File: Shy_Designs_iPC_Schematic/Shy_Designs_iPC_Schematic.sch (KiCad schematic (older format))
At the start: 1 part

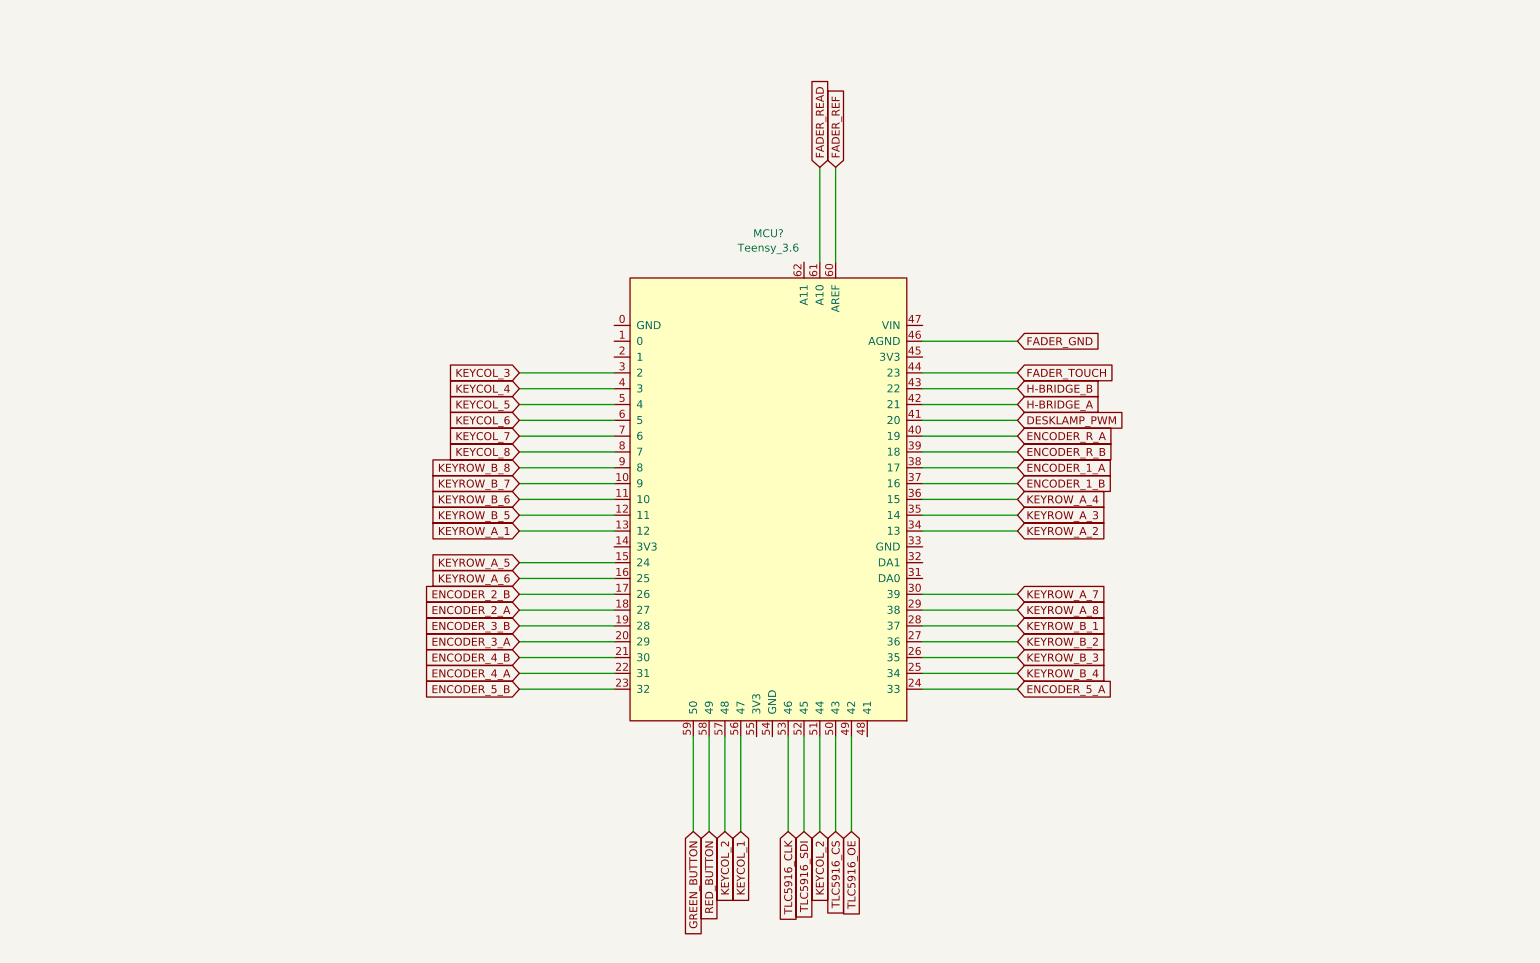
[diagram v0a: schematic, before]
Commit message: Correct schematic
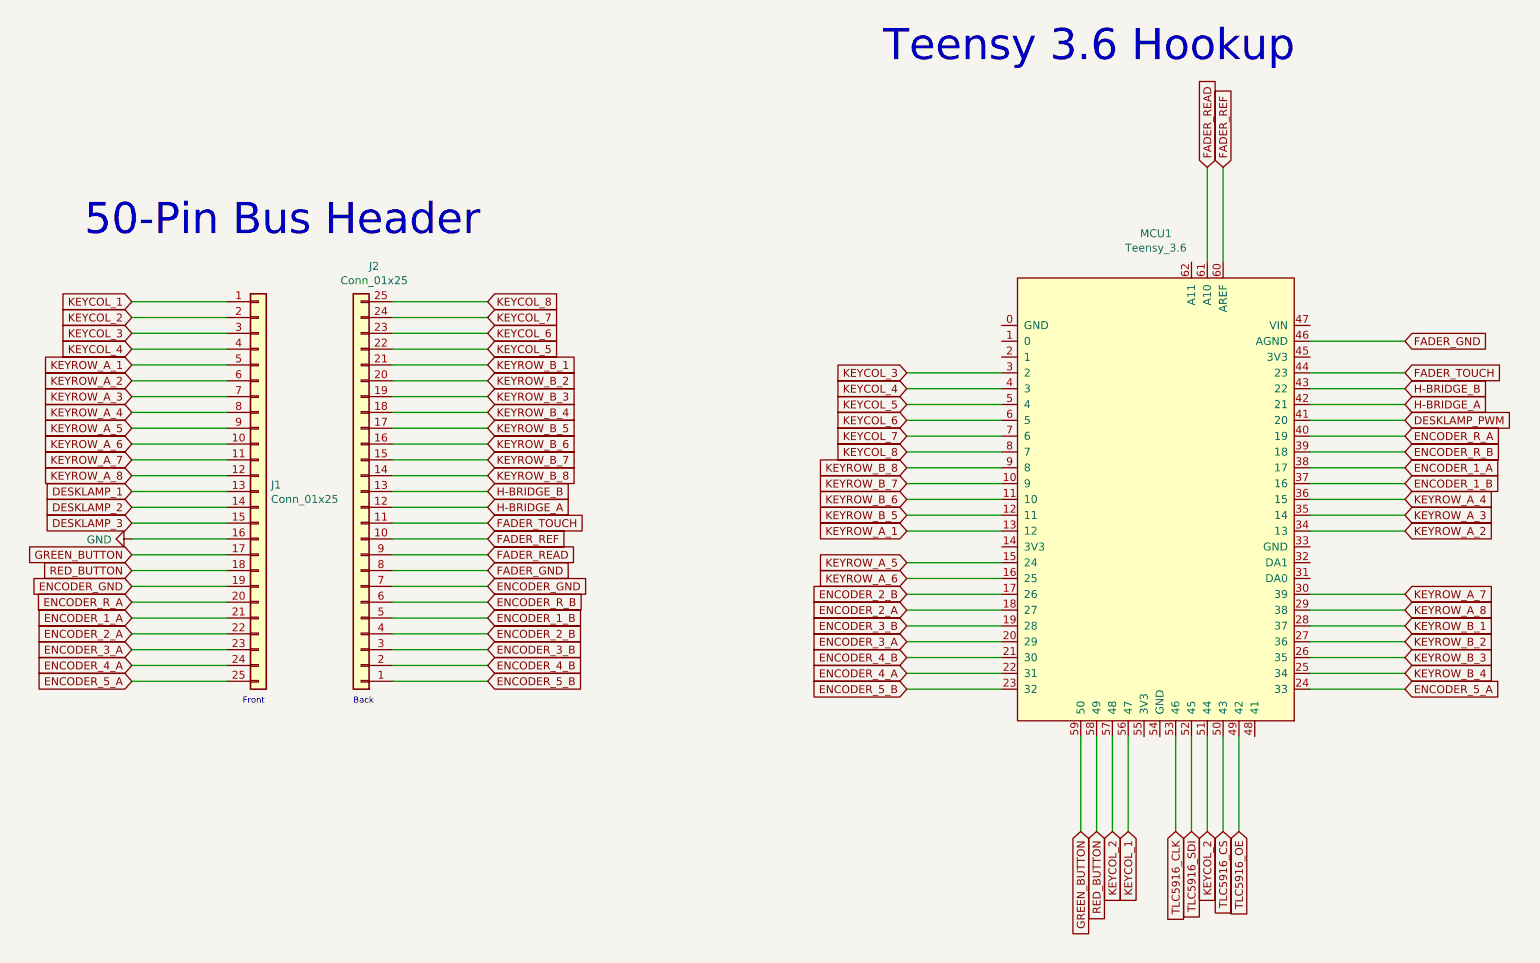
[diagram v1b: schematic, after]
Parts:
- added J1, J2: Conn_01x25, symbol Connector_Generic:Conn_01x25
- gave numbers to parts that had none: 1
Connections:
- net ENCODER_1_A: now also J1.21 (Pin_21)
- net ENCODER_1_B: now also J2.5 (Pin_5)
- net ENCODER_2_A: now also J1.22 (Pin_22)
- net ENCODER_2_B: now also J2.4 (Pin_4)
- net ENCODER_3_A: now also J1.23 (Pin_23)
- net ENCODER_3_B: now also J2.3 (Pin_3)
- net ENCODER_4_A: now also J1.24 (Pin_24)
- net ENCODER_4_B: now also J2.2 (Pin_2)
- net ENCODER_5_A: now also J1.25 (Pin_25)
- net ENCODER_5_B: now also J2.1 (Pin_1)
- net ENCODER_R_A: now also J1.20 (Pin_20)
- net ENCODER_R_B: now also J2.6 (Pin_6)
- net FADER_GND: now also J2.8 (Pin_8)
- net FADER_READ: now also J2.9 (Pin_9)
- net FADER_REF: now also J2.10 (Pin_10)
- net FADER_TOUCH: now also J2.11 (Pin_11)
- net GREEN_BUTTON: now also J1.17 (Pin_17)
- net H-BRIDGE_A: now also J2.12 (Pin_12)
- net H-BRIDGE_B: now also J2.13 (Pin_13)
- net KEYCOL_1: now also J1.1 (Pin_1)
- net KEYCOL_2: now also J1.2 (Pin_2)
- net KEYCOL_3: now also J1.3 (Pin_3)
- net KEYCOL_4: now also J1.4 (Pin_4)
- net KEYCOL_5: now also J2.22 (Pin_22)
- net KEYCOL_6: now also J2.23 (Pin_23)
- net KEYCOL_7: now also J2.24 (Pin_24)
- net KEYCOL_8: now also J2.25 (Pin_25)
- net KEYROW_A_1: now also J1.5 (Pin_5)
- net KEYROW_A_2: now also J1.6 (Pin_6)
- net KEYROW_A_3: now also J1.7 (Pin_7)
- net KEYROW_A_4: now also J1.8 (Pin_8)
- net KEYROW_A_5: now also J1.9 (Pin_9)
- net KEYROW_A_6: now also J1.10 (Pin_10)
- net KEYROW_A_7: now also J1.11 (Pin_11)
- net KEYROW_A_8: now also J1.12 (Pin_12)
- net KEYROW_B_1: now also J2.21 (Pin_21)
- net KEYROW_B_2: now also J2.20 (Pin_20)
- net KEYROW_B_3: now also J2.19 (Pin_19)
- net KEYROW_B_4: now also J2.18 (Pin_18)
- net KEYROW_B_5: now also J2.17 (Pin_17)
- net KEYROW_B_6: now also J2.16 (Pin_16)
- net KEYROW_B_7: now also J2.15 (Pin_15)
- net KEYROW_B_8: now also J2.14 (Pin_14)
- net RED_BUTTON: now also J1.18 (Pin_18)
- new net DESKLAMP_1: J1.13 (Pin_13)
- new net DESKLAMP_2: J1.14 (Pin_14)
- new net DESKLAMP_3: J1.15 (Pin_15)
- new net ENCODER_GND: J1.19 (Pin_19), J2.7 (Pin_7)
- new net GND: J1.16 (Pin_16)
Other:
- note added: "50-Pin Bus Header"
- note added: "Back"
- note added: "Front"
- note added: "Teensy 3.6 Hookup"
- moved on the sheet: MCU1
